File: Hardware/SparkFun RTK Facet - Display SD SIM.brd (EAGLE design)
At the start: 50 x 22 mm, 40 parts, among them J1 FPC_12_0.5MM2, J16 microSD, J17 NANO_SIM, J2 FPC_12_0.5MM2, U13 LIS2DH12

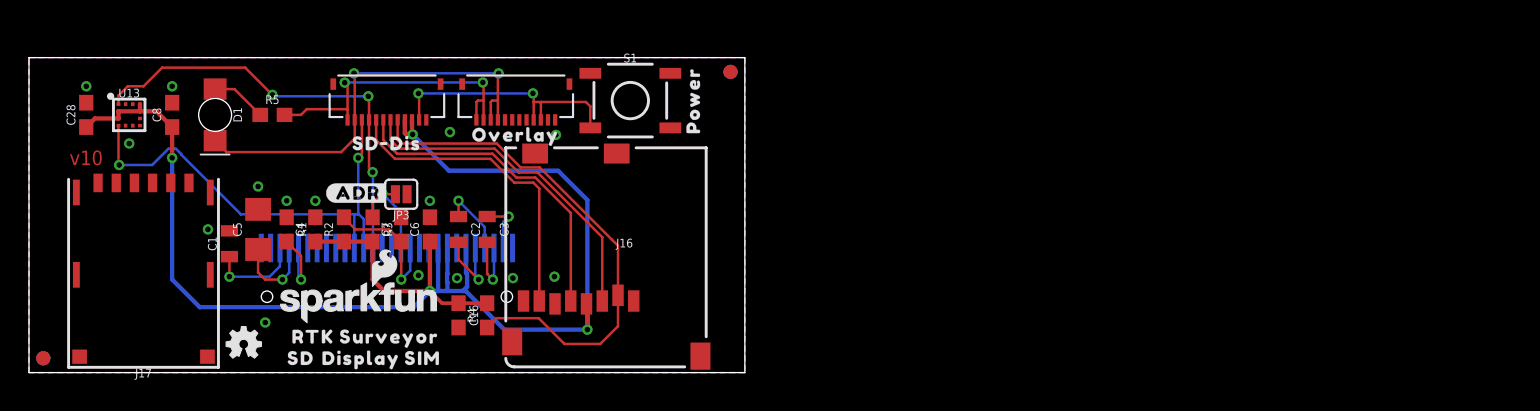
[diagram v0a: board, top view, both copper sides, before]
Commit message: Move display connector to side so overlay connector can be center. Notch PCBs. Add dummy PCB height. Add dummy retention plate.
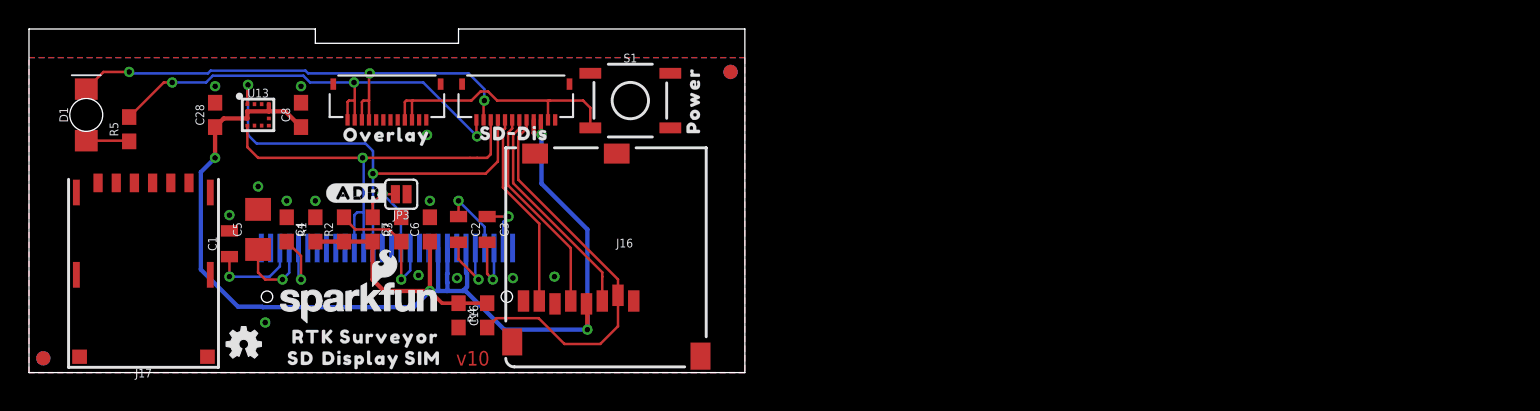
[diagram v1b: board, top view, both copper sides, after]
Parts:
- moved R5 10.0 mm to (7.00, 17.0), turned to 90 degrees
- moved C28 9.00 mm to (13.0, 18.0)
- moved C8 9.00 mm to (19.0, 18.0)
- moved D1 9.00 mm to (4.00, 18.0), turned to 90 degrees
- moved J1 9.00 mm to (34.0, 19.0)
- moved J2 9.00 mm to (25.0, 19.0)
- moved U$2 9.00 mm to (25.0, 16.6)
- moved U$8 9.00 mm to (4.00, 16.0)
- moved U13 9.00 mm to (16.0, 18.0)
- moved U$1 8.93 mm to (33.9, 16.7)
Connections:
- net VIN renamed V_USB
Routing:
- net V_USB: track 21.3 -> 32.8 mm, vias 2 -> 3
- net 3.3V: track 105.2 -> 95.0 mm
- net SD_CIPO: track 22.1 -> 13.8 mm
- net SD_SCK: track 22.8 -> 14.6 mm
- net SD_COPI: track 23.5 -> 15.4 mm
- net SD_!CS!: track 36.1 -> 28.2 mm
- net CHARGE_LED: track 30.2 -> 36.2 mm, vias 2 -> 3
- net ESP_21/SDA: track 33.5 -> 30.7 mm, vias 2 -> 1
- net ESP_22/SCL: track 30.4 -> 32.8 mm, vias 3 -> 2
- net N$3: track 3.90 -> 3.02 mm
- net POWER_BTN: track 18.6 -> 19.1 mm, vias 2 -> 0
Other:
- board size 50 x 22 mm -> 50 x 24 mm

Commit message: Adjust top edges for alignment.
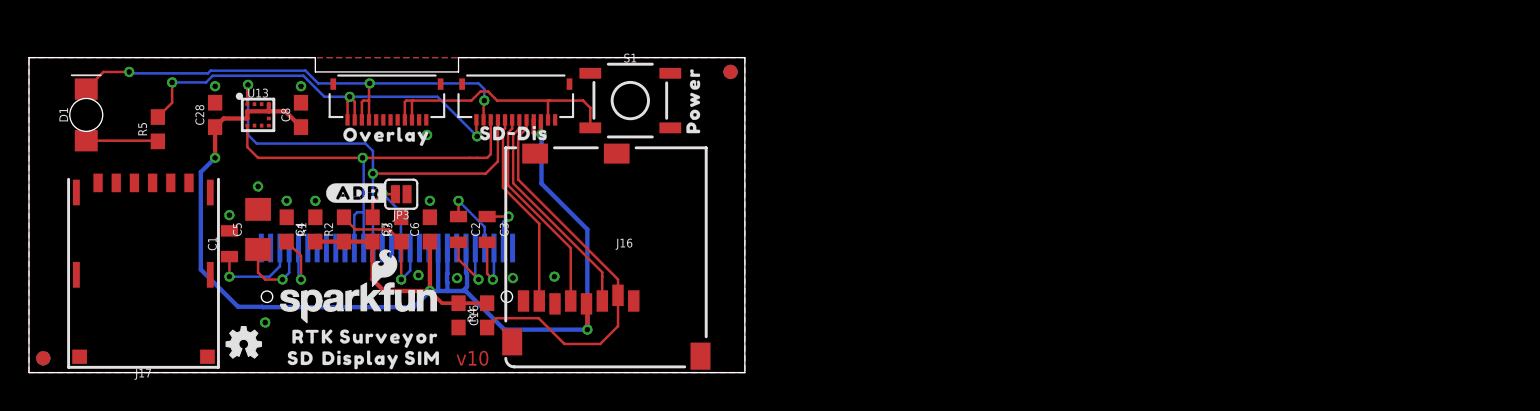
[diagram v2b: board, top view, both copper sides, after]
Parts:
- moved R5 2.00 mm to (9.00, 17.0)
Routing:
- net V_USB: track 32.8 -> 30.7 mm
- net N$3: track 3.02 -> 5.02 mm
- net CHARGE_LED: track 36.2 -> 35.5 mm
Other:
- board size 50 x 24 mm -> 50 x 22 mm
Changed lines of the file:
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@@
 <plain>
 <text x="31" y="1" size="1.016" layer="1" font="vector" ratio="20" rot="R180" align="center">v10</text>
-<wire x1="0" y1="0" x2="0" y2="24" width="0.05" layer="20"/>
-<wire x1="50" y1="24" x2="50" y2="0" width="0.05" layer="20"/>
+<wire x1="0" y1="0" x2="0" y2="22" width="0.05" layer="20"/>
+<wire x1="50" y1="22" x2="50" y2="0" width="0.05" layer="20"/>
 <wire x1="50" y1="0" x2="0" y2="0" width="0.05" layer="20"/>
 <rectangle x1="48" y1="0" x2="50" y2="22" layer="40" rot="R180"/>
@@
 <text x="59" y="21" size="0.5" layer="51" font="vector" ratio="15" align="center">FPC stiffener is 3mm</text>
 <dimension x1="51" y1="22" x2="51" y2="19" x3="53" y3="20.5" textsize="0.5" textratio="15" layer="51" width="0.05"/>
-<wire x1="20" y1="24" x2="0" y2="24" width="0.05" layer="20"/>
-<wire x1="30" y1="24" x2="50" y2="24" width="0.05" layer="20"/>
-<wire x1="30" y1="23" x2="30" y2="24" width="0.05" layer="20"/>
-<wire x1="20" y1="23" x2="20" y2="24" width="0.05" layer="20"/>
-<wire x1="30" y1="23" x2="20" y2="23" width="0.05" layer="20"/>
+<wire x1="20" y1="22" x2="0" y2="22" width="0.05" layer="20"/>
+<wire x1="30" y1="22" x2="50" y2="22" width="0.05" layer="20"/>
+<wire x1="30" y1="21" x2="30" y2="22" width="0.05" layer="20"/>
+<wire x1="20" y1="21" x2="20" y2="22" width="0.05" layer="20"/>
+<wire x1="30" y1="21" x2="20" y2="21" width="0.05" layer="20"/>
 </plain>
 <attributes>
@@
 <attribute name="VALUE" x="5.27" y="18" size="0.6096" layer="27" font="vector" ratio="20" rot="R90" align="top-center"/>
 </element>
-<element name="R5" library="SparkFun-Resistors" package="0603" value="1k" x="7" y="17" smashed="yes" rot="R90">
-<attribute name="NAME" x="6.238" y="17" size="0.6096" layer="25" font="vector" ratio="20" rot="R90" align="bottom-center"/>
-<attribute name="PROD_ID" value="RES-07856" x="7" y="17" size="1.778" layer="27" font="vector" ratio="15" rot="R90" display="off"/>
-<attribute name="VALUE" x="7.762" y="17" size="0.6096" layer="27" font="vector" ratio="20" rot="R90" align="top-center"/>
+<element name="R5" library="SparkFun-Resistors" package="0603" value="1k" x="9" y="17" smashed="yes" rot="R90">
+<attribute name="NAME" x="8.238" y="17" size="0.6096" layer="25" font="vector" ratio="20" rot="R90" align="bottom-center"/>
+<attribute name="PROD_ID" value="RES-07856" x="9" y="17" size="1.778" layer="27" font="vector" ratio="15" rot="R90" display="off"/>
+<attribute name="VALUE" x="9.762" y="17" size="0.6096" layer="27" font="vector" ratio="20" rot="R90" align="top-center"/>
 </element>
 <element name="J1" library="RTK Facet" package="FPC_12_FLIP_DOUBLESIDED_2" value="FPC_12_0.5MM2" x="34" y="19" smashed="yes" rot="R180"/>
@@
 <contactref element="D1" pad="A"/>
 <contactref element="R5" pad="1"/>
-<wire x1="4" y1="16.2" x2="6.95" y2="16.2" width="0.1778" layer="1"/>
-<wire x1="6.95" y1="16.2" x2="7" y2="16.15" width="0.1778" layer="1"/>
+<wire x1="4" y1="16.2" x2="8.95" y2="16.2" width="0.1778" layer="1"/>
+<wire x1="8.95" y1="16.2" x2="9" y2="16.15" width="0.1778" layer="1"/>
 </signal>
 <signal name="CHARGE_LED">
@@
 <contactref element="J2" pad="9"/>
 <wire x1="23.75" y1="17.65" x2="23.75" y2="19" width="0.1778" layer="1"/>
-<wire x1="23.75" y1="19" x2="23.75" y2="20.85" width="0.1778" layer="1"/>
-<wire x1="23.75" y1="20.85" x2="23.8" y2="20.9" width="0.1778" layer="1"/>
-<via x="23.8" y="20.9" extent="1-16" drill="0.381"/>
+<wire x1="23.75" y1="19" x2="23.75" y2="20.15" width="0.1778" layer="1"/>
+<wire x1="23.75" y1="20.15" x2="23.8" y2="20.2" width="0.1778" layer="1"/>
+<via x="23.8" y="20.2" extent="1-16" drill="0.381"/>
 <wire x1="23.25" y1="17.65" x2="23.25" y2="18.9" width="0.1778" layer="1"/>
 <wire x1="23.25" y1="18.9" x2="23.35" y2="19" width="0.1778" layer="1"/>
 <wire x1="23.35" y1="19" x2="23.75" y2="19" width="0.1778" layer="1"/>
-<wire x1="23.8" y1="20.9" x2="30.7" y2="20.9" width="0.1778" layer="16"/>
-<wire x1="30.7" y1="20.9" x2="31.8" y2="19.8" width="0.1778" layer="16"/>
+<wire x1="23.8" y1="20.2" x2="31.4" y2="20.2" width="0.1778" layer="16"/>
+<wire x1="31.4" y1="20.2" x2="31.8" y2="19.8" width="0.1778" layer="16"/>
 <wire x1="31.75" y1="17.65" x2="31.75" y2="18.95" width="0.1778" layer="1"/>
 <wire x1="31.75" y1="18.95" x2="31.8" y2="19" width="0.1778" layer="1"/>
@@
 <wire x1="7" y1="21" x2="5.2" y2="21" width="0.1778" layer="1"/>
 <wire x1="5.2" y1="21" x2="4" y2="19.8" width="0.1778" layer="1"/>
-<wire x1="23.8" y1="20.9" x2="19.50093125" y2="20.9" width="0.1778" layer="16"/>
-<wire x1="19.50093125" y1="20.9" x2="19.31033125" y2="21.0906" width="0.1778" layer="16"/>
+<wire x1="23.8" y1="20.2" x2="20.20093125" y2="20.2" width="0.1778" layer="16"/>
+<wire x1="20.20093125" y1="20.2" x2="19.31033125" y2="21.0906" width="0.1778" layer="16"/>
 <wire x1="19.31033125" y1="21.0906" x2="12.68966875" y2="21.0906" width="0.1778" layer="16"/>
 <wire x1="12.68966875" y1="21.0906" x2="12.49906875" y2="20.9" width="0.1778" layer="16"/>
@@
 <contactref element="J2" pad="12"/>
 <contactref element="J2" pad="11"/>
-<wire x1="22.75" y1="17.65" x2="22.75" y2="19" width="0.1778" layer="1"/>
-<wire x1="22.75" y1="19" x2="22.75" y2="20.215" width="0.1778" layer="1"/>
-<wire x1="22.75" y1="20.215" x2="22.7" y2="20.265" width="0.1778" layer="1"/>
-<via x="22.7" y="20.265" extent="1-16" drill="0.381"/>
-<wire x1="22.25" y1="17.65" x2="22.25" y2="18.9" width="0.1778" layer="1"/>
-<wire x1="22.25" y1="18.9" x2="22.35" y2="19" width="0.1778" layer="1"/>
-<wire x1="22.35" y1="19" x2="22.75" y2="19" width="0.1778" layer="1"/>
+<wire x1="22.75" y1="17.65" x2="22.75" y2="18.915" width="0.1778" layer="1"/>
+<via x="22.4" y="19.265" extent="1-16" drill="0.381"/>
+<wire x1="22.25" y1="18.9" x2="22.25" y2="17.65" width="0.1778" layer="1"/>
 <wire x1="31.25" y1="17.65" x2="31.25" y2="16.55" width="0.1778" layer="1"/>
 <wire x1="31.25" y1="16.55" x2="31.3" y2="16.5" width="0.1778" layer="1"/>
 <via x="31.3" y="16.5" extent="1-16" drill="0.381"/>
-<wire x1="31.3" y1="16.5" x2="27.535" y2="20.265" width="0.1778" layer="16"/>
-<wire x1="27.535" y1="20.265" x2="22.7" y2="20.265" width="0.1778" layer="16"/>
-<wire x1="7" y1="17.85" x2="9.415" y2="20.265" width="0.1778" layer="1"/>
-<wire x1="9.415" y1="20.265" x2="10" y2="20.265" width="0.1778" layer="1"/>
+<wire x1="31.3" y1="16.5" x2="28.535" y2="19.265" width="0.1778" layer="16"/>
+<wire x1="28.535" y1="19.265" x2="22.4" y2="19.265" width="0.1778" layer="16"/>
+<wire x1="10" y1="20.265" x2="10" y2="18.85" width="0.1778" layer="1"/>
+<wire x1="10" y1="18.85" x2="9" y2="17.85" width="0.1778" layer="1"/>
 <via x="10" y="20.265" extent="1-16" drill="0.381"/>
 <wire x1="10" y1="20.265" x2="12.36696875" y2="20.265" width="0.1778" layer="16"/>
-<wire x1="19.63303125" y1="20.265" x2="22.7" y2="20.265" width="0.1778" layer="16"/>
+<wire x1="20.63303125" y1="19.265" x2="22.4" y2="19.265" width="0.1778" layer="16"/>
 <wire x1="12.36696875" y1="20.265" x2="12.83696875" y2="20.735" width="0.1778" layer="16"/>
 <wire x1="12.83696875" y1="20.735" x2="19.16303125" y2="20.735" width="0.1778" layer="16"/>
-<wire x1="19.16303125" y1="20.735" x2="19.63303125" y2="20.265" width="0.1778" layer="16"/>
+<wire x1="19.16303125" y1="20.735" x2="20.63303125" y2="19.265" width="0.1778" layer="16"/>
+<wire x1="22.75" y1="18.915" x2="22.4" y2="19.265" width="0.1778" layer="1"/>
+<wire x1="22.4" y1="19.265" x2="22.4" y2="19.05" width="0.1778" layer="1"/>
+<wire x1="22.4" y1="19.05" x2="22.25" y2="18.9" width="0.1778" layer="1"/>
 </signal>
 </signals>

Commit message: Update PROD ID on 12 pin connector. Add gerbers for v10.
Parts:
- J1, J2: value FPC_12_0.5MM2 -> FPC_12_0.5MM_BACKFLIP; device RTK Facet:FPC_12_FLIP_DOUBLESIDED_2 -> RTK Facet:FPC_12_DOUBLESIDED_BACKFLIP
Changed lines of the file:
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@@
 <attribute name="VALUE" x="9.762" y="17" size="0.6096" layer="27" font="vector" ratio="20" rot="R90" align="top-center"/>
 </element>
-<element name="J1" library="RTK Facet" package="FPC_12_FLIP_DOUBLESIDED_2" value="FPC_12_0.5MM2" x="34" y="19" smashed="yes" rot="R180"/>
+<element name="J1" library="RTK Facet" package="FPC_12_DOUBLESIDED_BACKFLIP" value="FPC_12_0.5MM_BACKFLIP" x="34" y="19" smashed="yes" rot="R180">
+<attribute name="PROD_ID" value="CONN-15766" x="34" y="19" size="1.778" layer="27" rot="R180" display="off"/>
+</element>
 <element name="U$1" library="output" package="SD#DIS0" value="" x="33.9" y="16.7" smashed="yes"/>
 <element name="U13" library="SparkFun-Sensors" package="LGA-12-LISDH12" value="LIS2DH12" x="16" y="18" smashed="yes">
@@
 <attribute name="VALUE" x="8" y="7" size="0.6096" layer="27" font="vector" ratio="20" align="top-center"/>
 </element>
-<element name="J2" library="RTK Facet" package="FPC_12_FLIP_DOUBLESIDED_2" value="FPC_12_0.5MM2" x="25" y="19" smashed="yes" rot="R180"/>
+<element name="J2" library="RTK Facet" package="FPC_12_DOUBLESIDED_BACKFLIP" value="FPC_12_0.5MM_BACKFLIP" x="25" y="19" smashed="yes" rot="R180">
+<attribute name="PROD_ID" value="CONN-15766" x="25" y="19" size="1.778" layer="27" rot="R180" display="off"/>
+</element>
 <element name="S1" library="SparkFun-Switches" package="TACTILE_SWITCH_SMD_5.2MM" value="" x="42" y="19" smashed="yes">
 <attribute name="NAME" x="42" y="21.667" size="0.6096" layer="25" font="vector" ratio="20" align="bottom-center"/>
@@
 <via x="16" y="13" extent="1-16" drill="0.381"/>
 <via x="19" y="20" extent="1-16" drill="0.381"/>
+<wire x1="36.75" y1="17.65" x2="39.206" y2="20.905" width="0" layer="19" extent="1-1"/>
+<wire x1="35.35" y1="15.3" x2="36.75" y2="17.65" width="0" layer="19" extent="1-1"/>
+<wire x1="33.775" y1="8.7" x2="35.35" y2="15.3" width="0" layer="19" extent="1-16"/>
+<wire x1="33.8" y1="6.6" x2="33.775" y2="8.7" width="0" layer="19" extent="16-16"/>
+<wire x1="36.7" y1="6.7" x2="33.8" y2="6.6" width="0" layer="19" extent="1-1"/>
+<wire x1="36.74" y1="4.8" x2="36.7" y2="6.7" width="0" layer="19" extent="1-1"/>
+<wire x1="29.875" y1="8.7" x2="33.775" y2="8.7" width="0" layer="19" extent="16-16"/>
+<wire x1="27.925" y1="8.7" x2="29.875" y2="8.7" width="0" layer="19" extent="16-16"/>
+<wire x1="27.2" y1="6.8" x2="27.925" y2="8.7" width="0" layer="19" extent="16-16"/>
+<wire x1="29.9" y1="6.6" x2="29.875" y2="8.7" width="0" layer="19" extent="16-16"/>
+<wire x1="28" y1="10.85" x2="27.925" y2="8.7" width="0" layer="19" extent="1-16"/>
+<wire x1="28" y1="12" x2="28" y2="10.85" width="0" layer="19" extent="1-1"/>
+<wire x1="26.4064" y1="12.46" x2="28" y2="12" width="0" layer="19" extent="1-1"/>
+<wire x1="26" y1="10.85" x2="26.4064" y2="12.46" width="0" layer="19" extent="1-1"/>
+<wire x1="30" y1="3.15" x2="29.9" y2="6.6" width="0" layer="19" extent="1-1"/>
+<wire x1="33.75" y1="2.15" x2="30" y2="3.15" width="0" layer="19" extent="1-1"/>
+<wire x1="27.8" y1="16.6" x2="26.4064" y2="12.46" width="0" layer="19" extent="1-1"/>
+<wire x1="27.75" y1="17.65" x2="27.8" y2="16.6" width="0" layer="19" extent="1-1"/>
+<wire x1="27.25" y1="17.65" x2="27.75" y2="17.65" width="0" layer="19" extent="1-1"/>
+<wire x1="20" y1="10.85" x2="26" y2="10.85" width="0" layer="19" extent="1-1"/>
+<wire x1="20" y1="12" x2="20" y2="10.85" width="0" layer="19" extent="1-1"/>
+<wire x1="18" y1="10.85" x2="20" y2="10.85" width="0" layer="19" extent="1-1"/>
+<wire x1="18" y1="12" x2="18" y2="10.85" width="0" layer="19" extent="1-1"/>
+<wire x1="16" y1="11.4" x2="18" y2="10.85" width="0" layer="19" extent="1-1"/>
+<wire x1="16" y1="13" x2="16" y2="11.4" width="0" layer="19" extent="1-1"/>
+<wire x1="14" y1="11" x2="16" y2="11.4" width="0" layer="19" extent="1-1"/>
+<wire x1="14" y1="9.9" x2="14" y2="11" width="0" layer="19" extent="1-1"/>
+<wire x1="16.875" y1="8.7" x2="18" y2="10.85" width="0" layer="19" extent="1-16"/>
+<wire x1="16.225" y1="8.7" x2="16.875" y2="8.7" width="0" layer="19" extent="16-16"/>
+<wire x1="16.25" y1="17.25" x2="16" y2="13" width="0" layer="19" extent="1-1"/>
+<wire x1="16.75" y1="17.25" x2="16.25" y2="17.25" width="0" layer="19" extent="1-1"/>
+<wire x1="16.75" y1="17.75" x2="16.75" y2="17.25" width="0" layer="19" extent="1-1"/>
+<wire x1="15.75" y1="17.25" x2="16.25" y2="17.25" width="0" layer="19" extent="1-1"/>
+<wire x1="19" y1="18.85" x2="16.75" y2="17.75" width="0" layer="19" extent="1-1"/>
+<wire x1="19" y1="20" x2="19" y2="18.85" width="0" layer="19" extent="1-1"/>
+<wire x1="13" y1="18.85" x2="15.75" y2="17.25" width="0" layer="19" extent="1-1"/>
+<wire x1="13" y1="20" x2="13" y2="18.85" width="0" layer="19" extent="1-1"/>
+<wire x1="16.5" y1="3.5" x2="16.875" y2="8.7" width="0" layer="19" extent="16-16"/>
+<wire x1="46.9" y1="1.15" x2="36.74" y2="4.8" width="0" layer="19" extent="1-1"/>
 </signal>
 <signal name="VCOMH">

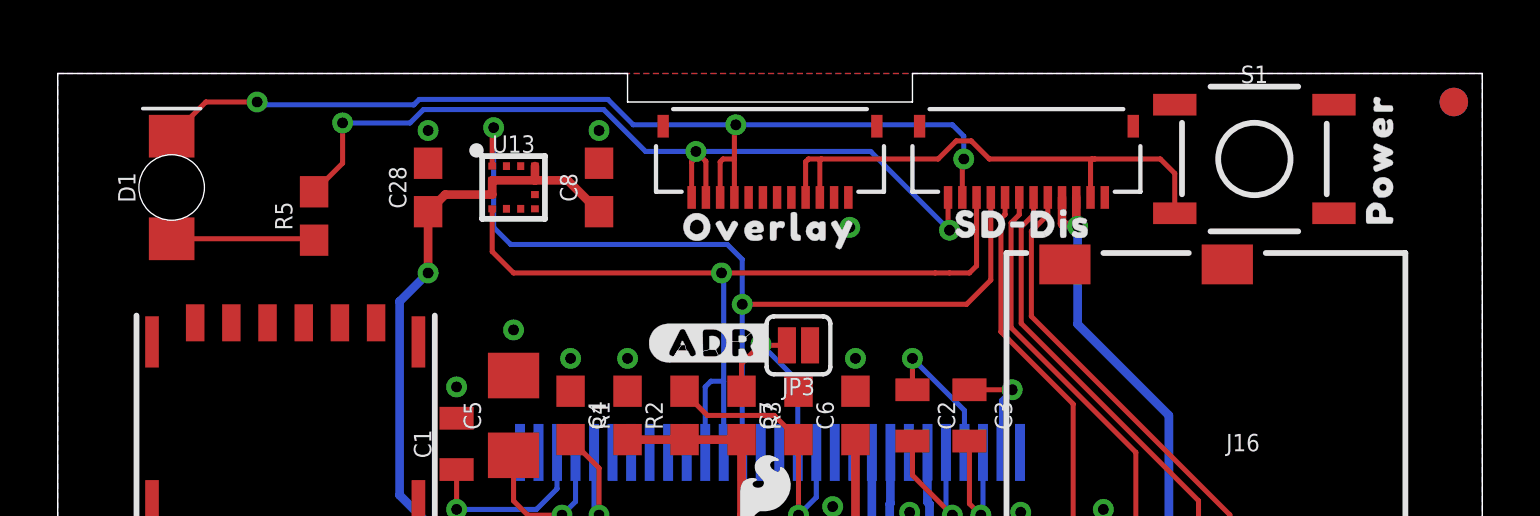
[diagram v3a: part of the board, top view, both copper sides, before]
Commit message: Moved power LED to left side of front display.
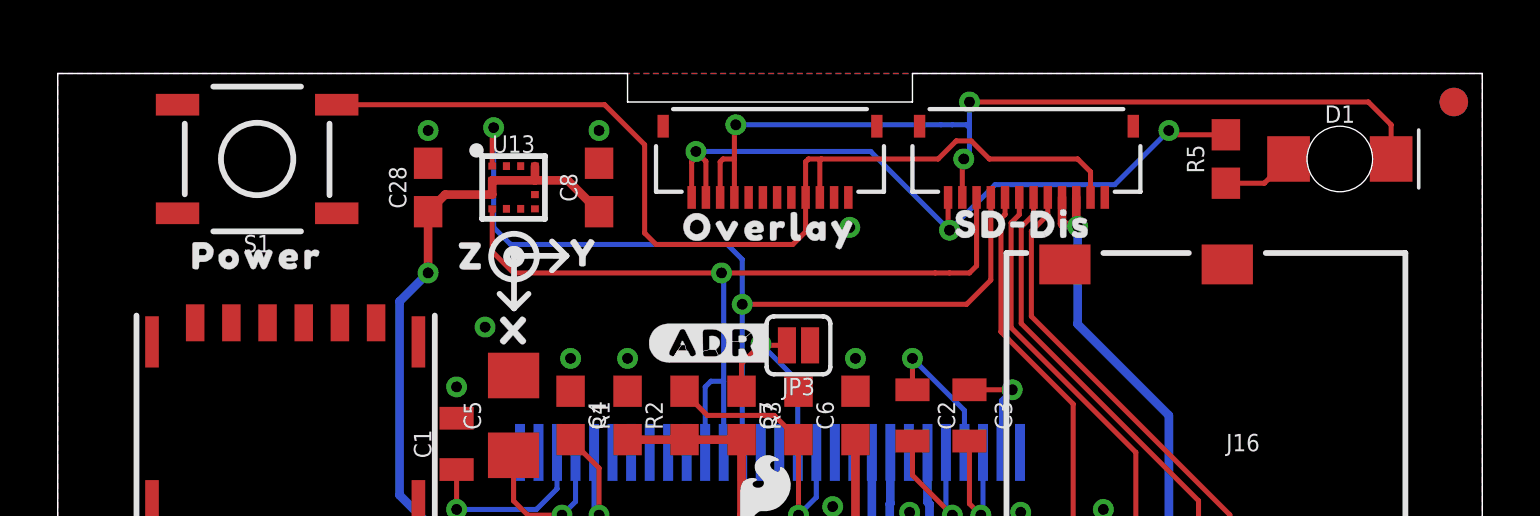
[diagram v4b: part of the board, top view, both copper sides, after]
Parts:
- added U$10: (no value), output:X0
- added U$11: (no value), output:Y1
- added U$12: (no value), output:Z2
- moved D1 41.0 mm to (45.0, 19.0), turned to 0 degrees
- moved U$8 41.0 mm to (45.0, 17.0)
- moved U$9 39.5 mm to (7.00, 15.6), turned to 0 degrees
- moved S1 35.0 mm to (7.00, 19.0), turned to 180 degrees
- moved R5 32.1 mm to (41.0, 19.0)
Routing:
- net POWER_BTN: track 19.1 -> 36.0 mm
- net V_USB: track 30.7 -> 25.9 mm
- net CHARGE_LED: track 35.5 -> 32.4 mm
- net N$3: track 5.02 -> 2.55 mm
